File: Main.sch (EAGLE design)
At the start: 32 parts, among them IC1 MSGEQ7, IC2 LM358N, IC3 LM358N, IC4 LM358N, IC5 LM358N, T1 2SC3631, T2 2SC3631, T3 2SC3631, T4 2SC3631, T5 2SC3631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

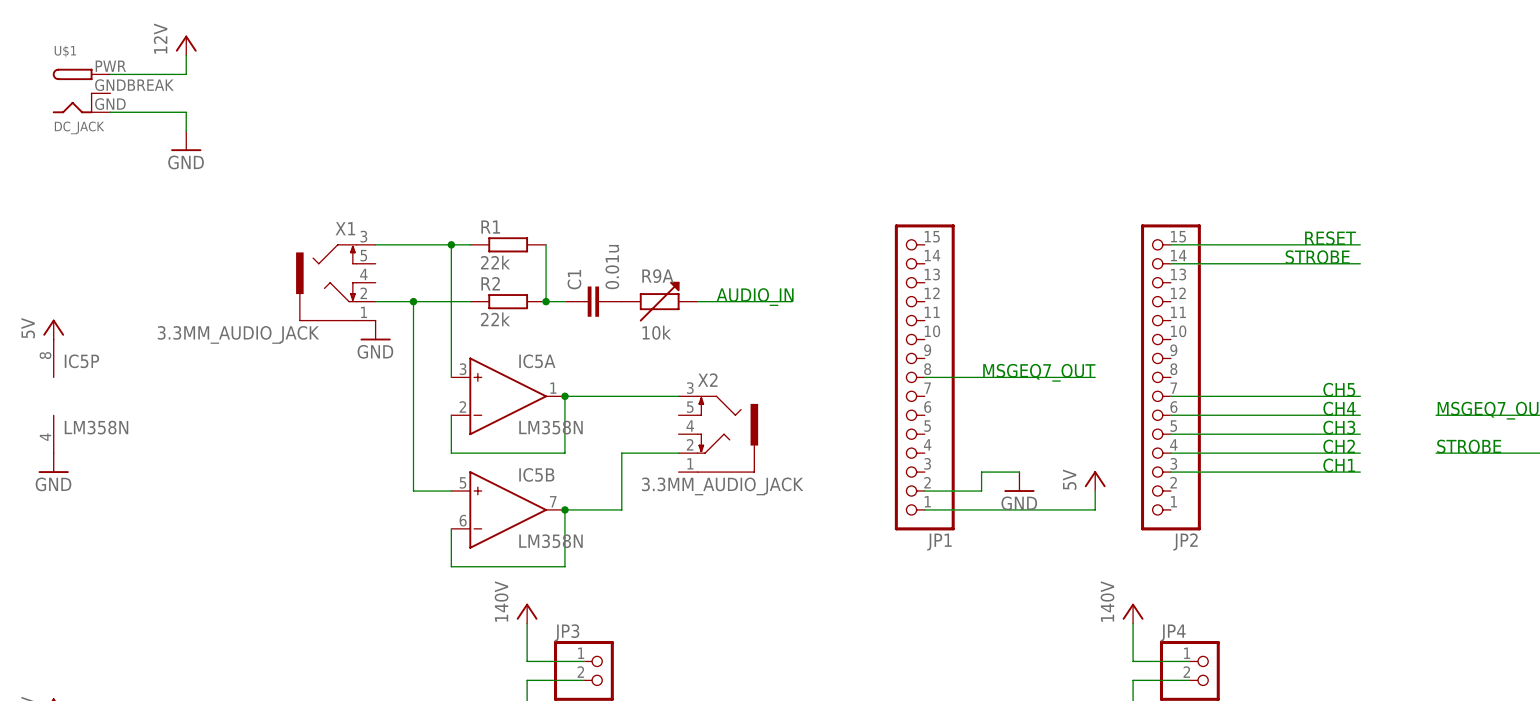
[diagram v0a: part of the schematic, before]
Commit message: [add]電源の追加
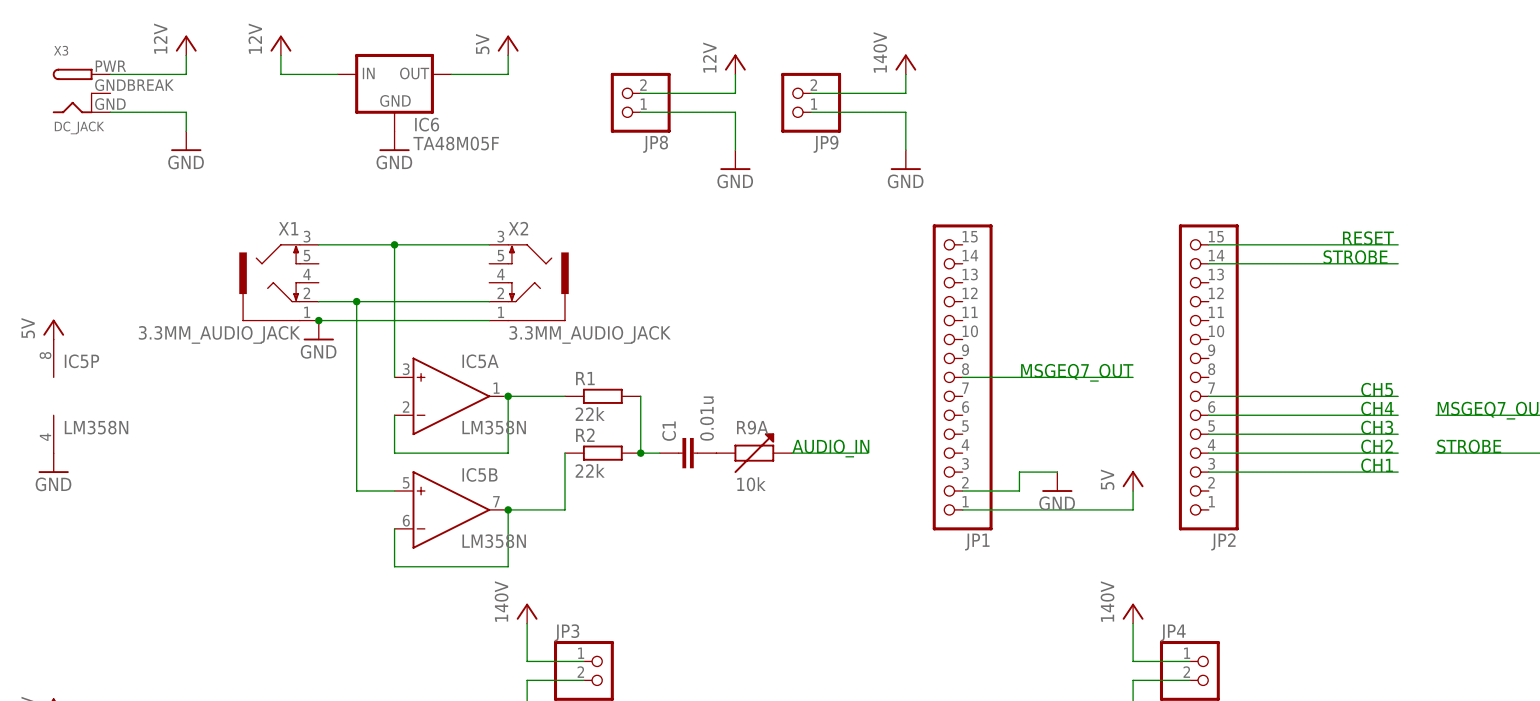
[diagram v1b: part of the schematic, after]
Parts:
- added IC6: TA48M05F, SpectralAnalyzer:TA48M05F
- added JP8, JP9: (no value), SpectralAnalyzer:PINHD-1X2
- renumbered U$1 to X3
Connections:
- net GND: now also IC6.GND, JP8.1, JP9.1, X2.1
- net N$2: now also X2.3; no longer R1.1
- net N$3: now also X2.2; no longer R2.1
- net N$39: now also R1.1; no longer X2.3
- net N$42: now also R2.1; no longer X2.2
- net VCC: now also IC6.IN, IC6.OUT, JP8.2, JP9.2
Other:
- moved on the sheet: C1, IC5A, IC5B, JP1, JP2, R1, R2, R9A, X1, X2
